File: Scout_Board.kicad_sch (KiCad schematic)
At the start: 0 parts

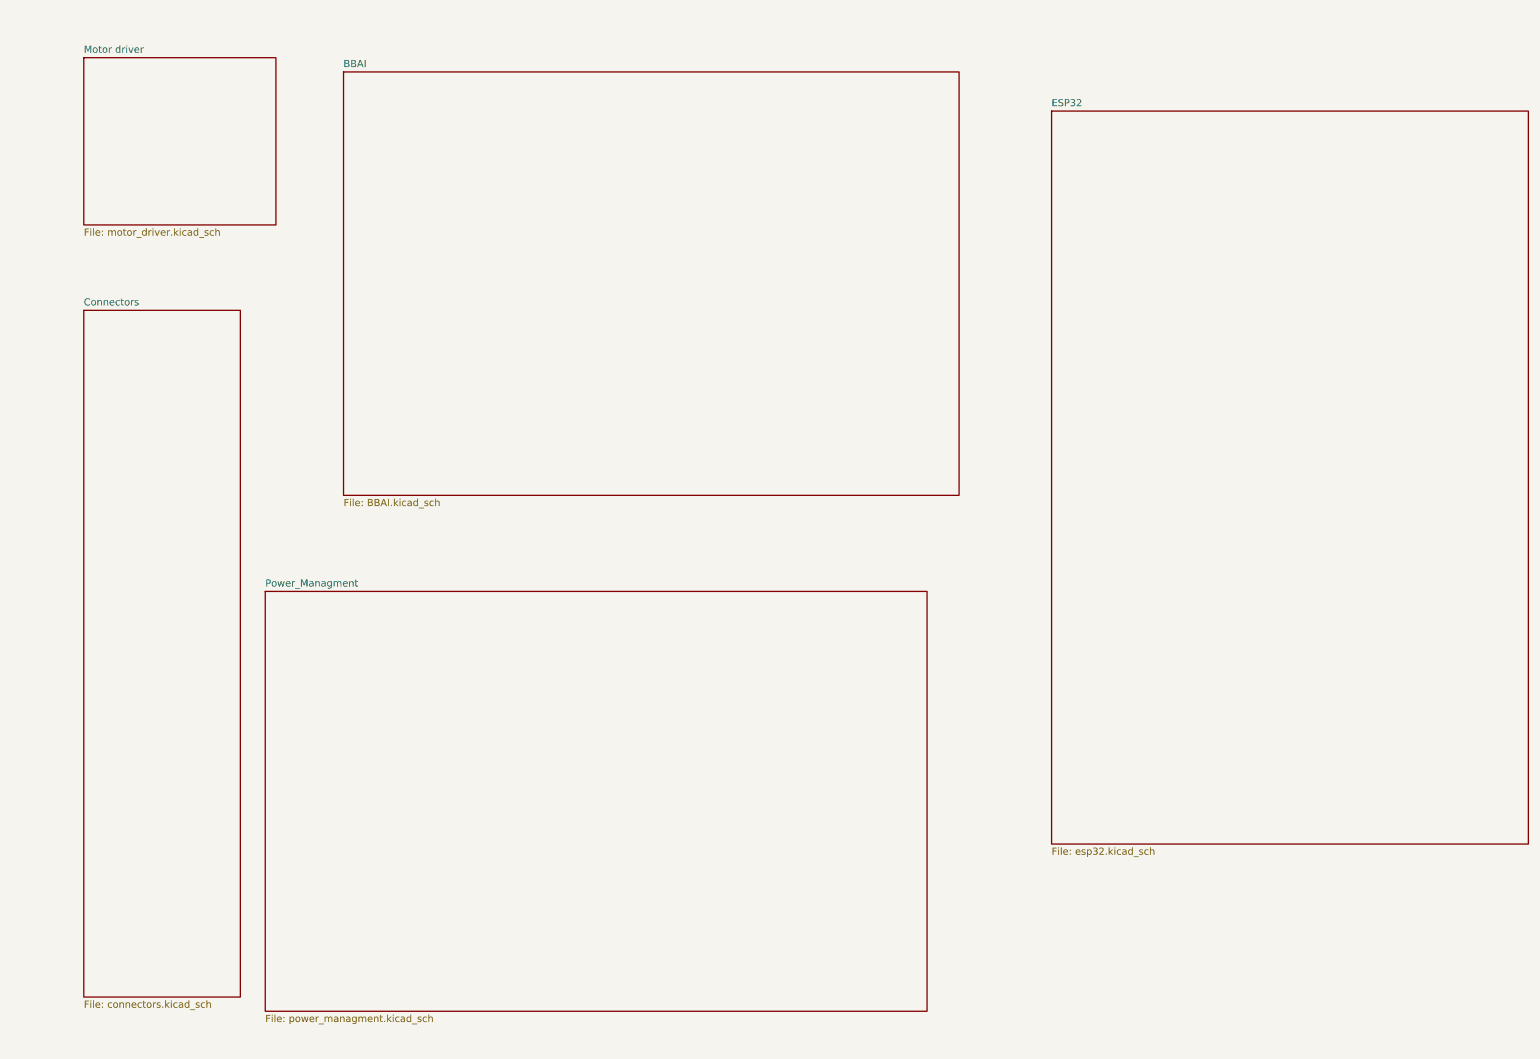
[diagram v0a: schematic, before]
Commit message: Base changes
Deleted the redundant files.
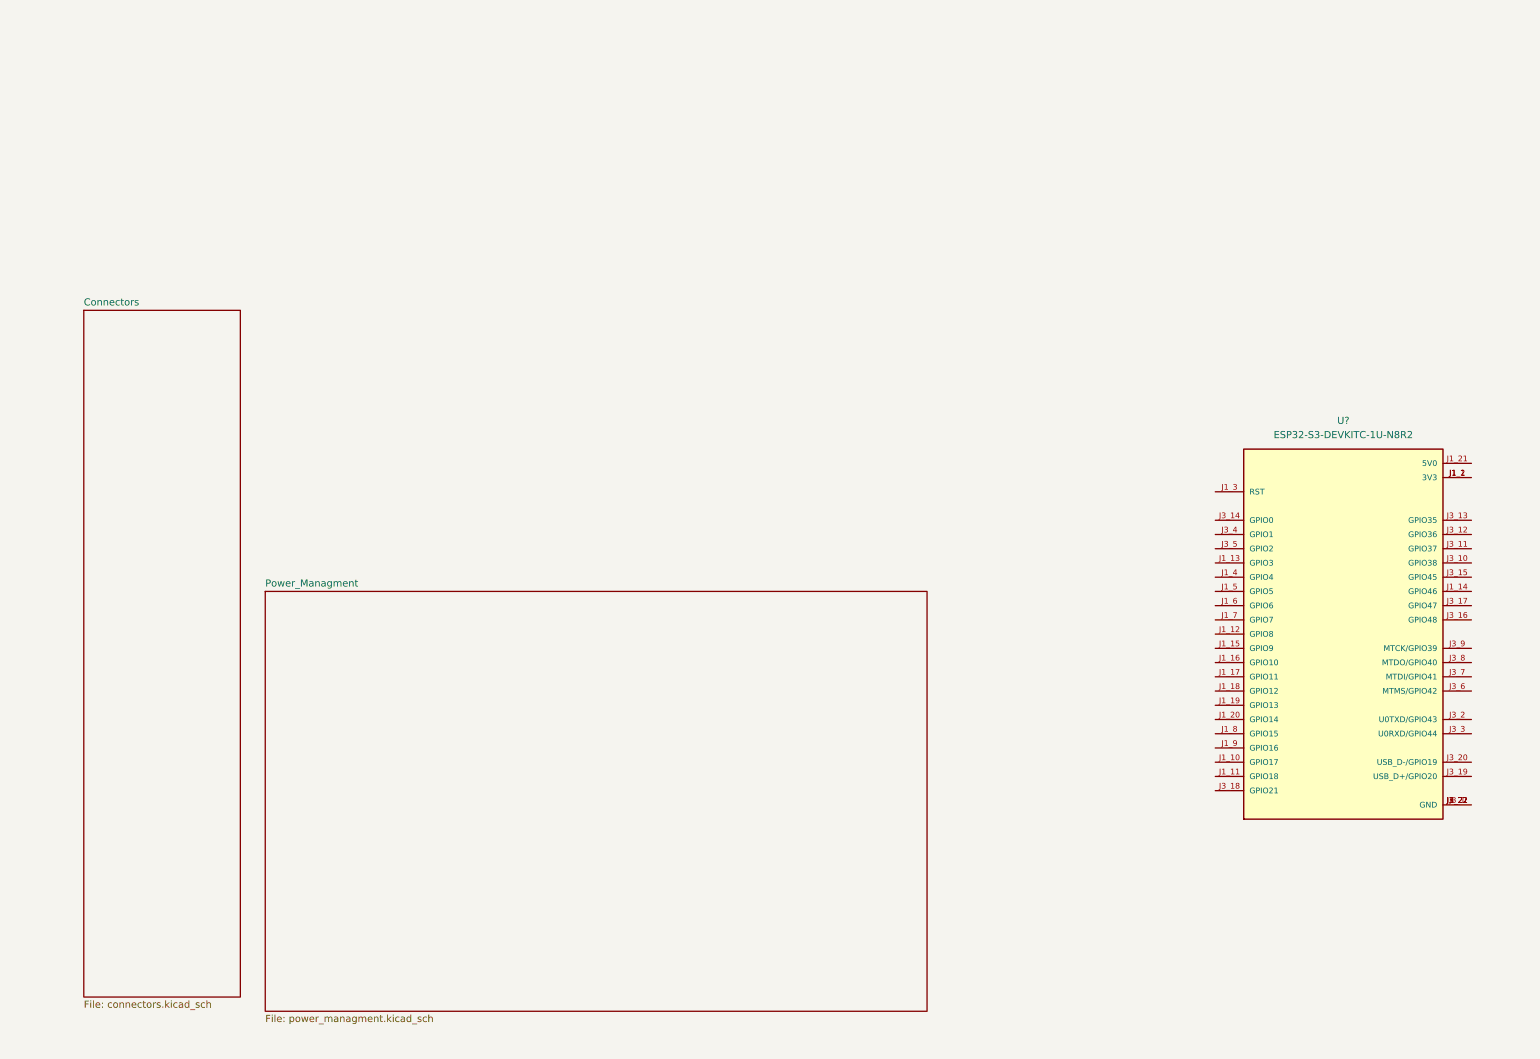
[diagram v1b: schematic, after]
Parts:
- added U?: ESP32-S3-DEVKITC-1U-N8R2, ESP32-S3-DEVKITC-1U-N8R2:XCVR_ESP32-S3-DEVKITC-1U-N8R2, symbol ESP32-S3-DEVKITC-1U-N8R2:ESP32-S3-DEVKITC-1U-N8R2
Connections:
- new net: U?.J1_1 (3V3), U?.J1_2 (3V3)
- new net: U?.J1_22 (GND), U?.J3_1 (GND), U?.J3_21 (GND), U?.J3_22 (GND)
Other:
- removed sheet BBAI
- removed sheet ESP32
- removed sheet Motor driver
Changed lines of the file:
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@@
 (kicad_sch (version 20230121) (generator eeschema)
   (paper "A4")
-  (sheet (at 191.77 28.575) (size 85.09 130.81) (fields_autoplaced)
-    (stroke (width 0.1524) (type solid))
-    (fill (color 0 0 0 0.0000))
-    (property "Sheetname" "ESP32" (at 191.77 27.8634 0)
-      (effects (font (size 1.27 1.27)) (justify left bottom))
+  (symbol (lib_id "ESP32-S3-DEVKITC-1U-N8R2:ESP32-S3-DEVKITC-1U-N8R2") (at 243.84 121.92 0) (unit 1)
+    (in_bom yes) (on_board yes) (dnp no) (fields_autoplaced)
+    (property "Reference" "U?" (at 243.84 83.82 0)
+      (effects (font (size 1.27 1.27)))
     )
-    (property "Sheetfile" "esp32.kicad_sch" (at 191.77 159.9696 0)
-      (effects (font (size 1.27 1.27)) (justify left top))
+    (property "Value" "ESP32-S3-DEVKITC-1U-N8R2" (at 243.84 86.36 0)
+      (effects (font (size 1.27 1.27)))
     )
+    (property "Footprint" "ESP32-S3-DEVKITC-1U-N8R2:XCVR_ESP32-S3-DEVKITC-1U-N8R2" (at 243.84 121.92 0)
+      (effects (font (size 1.27 1.27)) (justify bottom) hide)
+    )
+    (property "Datasheet" "" (at 243.84 121.92 0)
+      (effects (font (size 1.27 1.27)) hide)
+    )
+    (property "MF" "Espressif Systems" (at 243.84 121.92 0)
+      (effects (font (size 1.27 1.27)) (justify bottom) hide)
+    )
+    (property "MAXIMUM_PACKAGE_HEIGHT" "10.69mm" (at 243.84 121.92 0)
+      (effects (font (size 1.27 1.27)) (justify bottom) hide)
+    )
+    (property "Package" "None" (at 243.84 121.92 0)
+      (effects (font (size 1.27 1.27)) (justify bottom) hide)
+    )
+    (property "Price" "None" (at 243.84 121.92 0)
+      (effects (font (size 1.27 1.27)) (justify bottom) hide)
+    )
+    (property "Check_prices" "https://www.snapeda.com/parts/ESP32-S3-DEVKITC-1U-N8R2/Espressif+Systems/view-part/?ref=eda" (at 243.84 121.92 0)
+      (effects (font (size 1.27 1.27)) (justify bottom) hide)
+    )
+    (property "STANDARD" "Manufacturer Recommendations" (at 243.84 121.92 0)
+      (effects (font (size 1.27 1.27)) (justify bottom) hide)
+    )
+    (property "PARTREV" "5.3" (at 243.84 121.92 0)
+      (effects (font (size 1.27 1.27)) (justify bottom) hide)
+    )
+    (property "SnapEDA_Link" "https://www.snapeda.com/parts/ESP32-S3-DEVKITC-1U-N8R2/Espressif+Systems/view-part/?ref=snap" (at 243.84 121.92 0)
+      (effects (font (size 1.27 1.27)) (justify bottom) hide)
+    )
+    (property "MP" "ESP32-S3-DEVKITC-1U-N8R2" (at 243.84 121.92 0)
+      (effects (font (size 1.27 1.27)) (justify bottom) hide)
+    )
+    (property "Purchase-URL" "https://www.snapeda.com/api/url_track_click_mouser/?unipart_id=12089198&manufacturer=Espressif Systems&part_name=ESP32-S3-DEVKITC-1U-N8R2&search_term=esp32-s3-devkitc-1u" (at 243.84 121.92 0)
+      (effects (font (size 1.27 1.27)) (justify bottom) hide)
+    )
+    (property "Description" "\nWiFi Development Tools - 802.11 ESP32-S3 Gen-Purpose Dev Bd, embeds ESP32-S3-WROOM-1U-N8R2, 8 MB Quad Flash, 2 MB Quad PSRAM, IPEX antenna connector, w/ Pin Header\n" (at 243.84 121.92 0)
+      (effects (font (size 1.27 1.27)) (justify bottom) hide)
+    )
+    (property "Availability" "In Stock" (at 243.84 121.92 0)
+      (effects (font (size 1.27 1.27)) (justify bottom) hide)
+    )
+    (property "MANUFACTURER" "Espressif" (at 243.84 121.92 0)
+      (effects (font (size 1.27 1.27)) (justify bottom) hide)
+    )
+    (pin "J1_10")
+    (pin "J3_18")
+    (pin "J3_7")
+    (pin "J3_4")
+    (pin "J1_13")
+    (pin "J3_3")
+    (pin "J3_15")
+    (pin "J3_11")
+    (pin "J3_16")
+    (pin "J1_8")
+    (pin "J3_19")
+    (pin "J3_2")
+    (pin "J1_3")
+    (pin "J3_9")
+    (pin "J3_6")
+    (pin "J3_17")
+    (pin "J3_22")
+    (pin "J1_4")
+    (pin "J3_1")
+    (pin "J1_14")
+    (pin "J1_20")
+    (pin "J1_5")
+    (pin "J1_18")
+    (pin "J1_2")
+    (pin "J1_16")
+    (pin "J1_17")
+    (pin "J3_14")
+    (pin "J3_12")
+    (pin "J1_7")
+    (pin "J3_20")
+    (pin "J1_11")
+    (pin "J1_15")
+    (pin "J1_19")
+    (pin "J1_12")
+    (pin "J1_21")
+    (pin "J3_5")
+    (pin "J1_22")
+    (pin "J3_8")
+    (pin "J3_10")
+    (pin "J1_9")
+    (pin "J3_13")
+    (pin "J1_6")
+    (pin "J1_1")
+    (pin "J3_21")
     (instances
       (project "Scout_Board"
-        (path "/e58a9779-147f-4c0c-a745-6e9bc8ec0357" (page "4"))
+        (path "/e58a9779-147f-4c0c-a745-6e9bc8ec0357"
+          (reference "U?") (unit 1)
+        )
       )
     )
@@
     )
   )
-  (sheet (at 19.05 19.05) (size 34.29 29.845) (fields_autoplaced)
-    (stroke (width 0.1524) (type solid))
-    (fill (color 0 0 0 0.0000))
-    (property "Sheetname" "Motor driver" (at 19.05 18.3384 0)
-      (effects (font (size 1.27 1.27)) (justify left bottom))
-    )
-    (property "Sheetfile" "motor_driver.kicad_sch" (at 19.05 49.4796 0)
-      (effects (font (size 1.27 1.27)) (justify left top))
-    )
-    (instances
-      (project "Scout_Board"
-        (path "/e58a9779-147f-4c0c-a745-6e9bc8ec0357" (page "6"))
-      )
-    )
-  )
   (sheet (at 19.05 64.135) (size 27.94 122.555) (fields_autoplaced)
     (stroke (width 0.1524) (type solid))
@@
       )
     )
-  )
-  (sheet (at 65.405 21.59) (size 109.855 75.565) (fields_autoplaced)
-    (stroke (width 0.1524) (type solid))
-    (fill (color 0 0 0 0.0000))
-    (property "Sheetname" "BBAI" (at 65.405 20.8784 0)
-      (effects (font (size 1.27 1.27)) (justify left bottom))
-    )
-    (property "Sheetfile" "BBAI.kicad_sch" (at 65.405 97.7396 0)
-      (effects (font (size 1.27 1.27)) (justify left top))
-    )
-    (instances
-      (project "Scout_Board"
-        (path "/e58a9779-147f-4c0c-a745-6e9bc8ec0357" (page "2"))
-      )
-    )

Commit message: In process of adding top and bottom lights
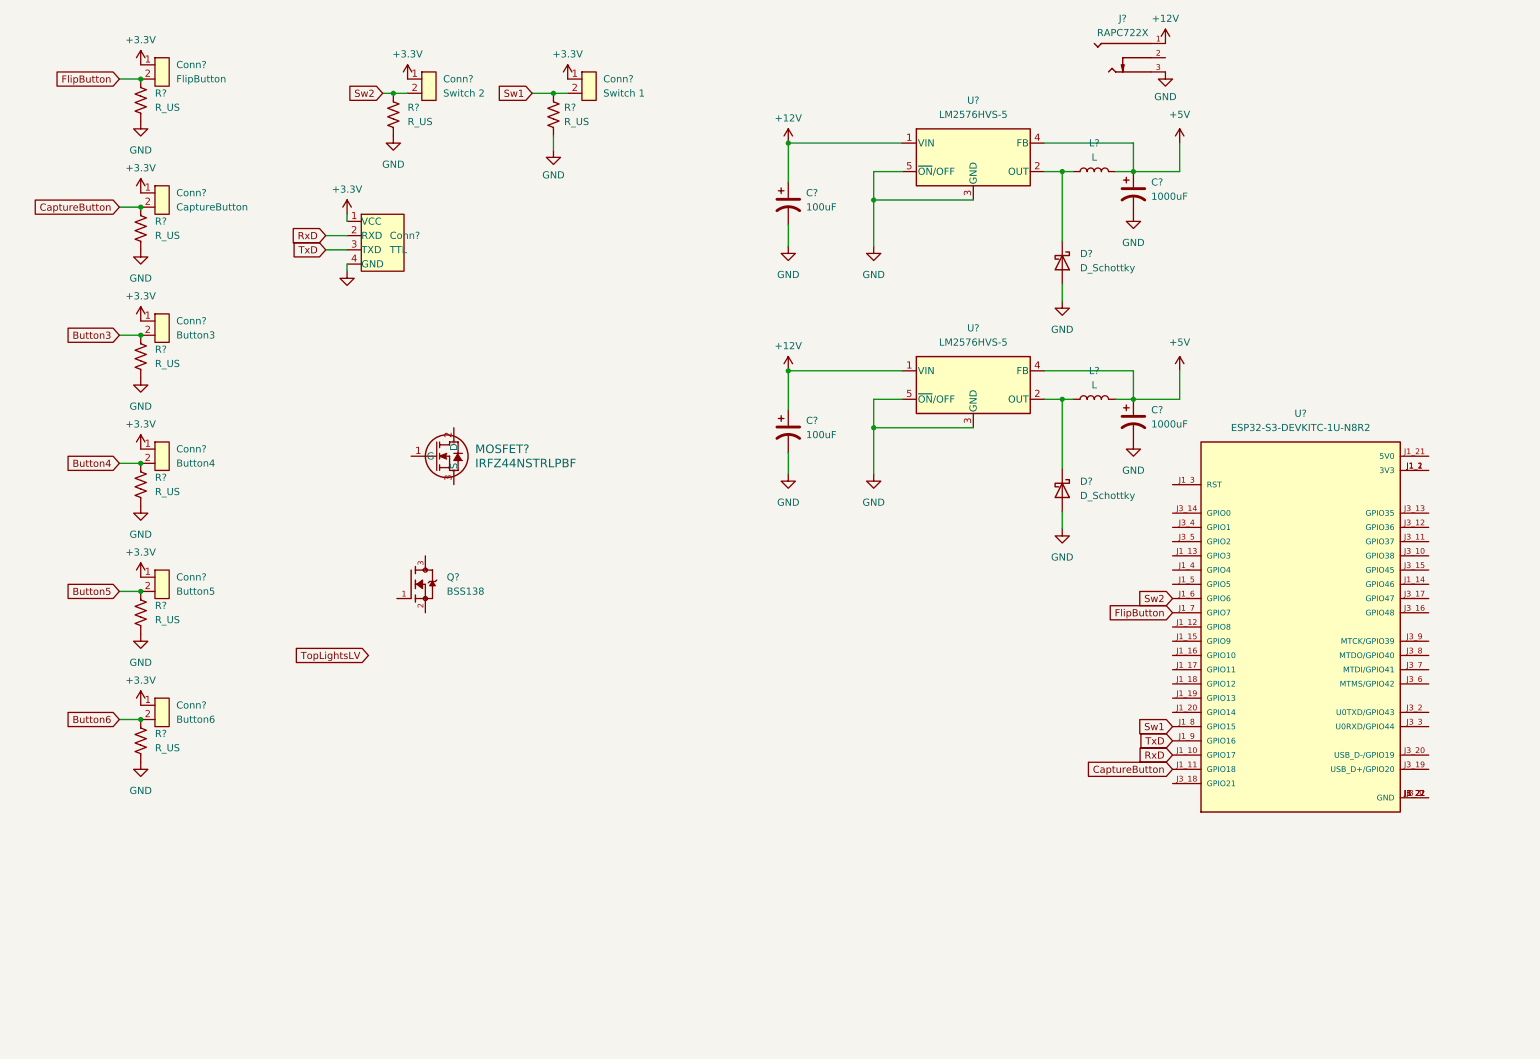
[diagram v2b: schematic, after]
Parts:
- added C? (x2): 100uF, symbol Device:C_Polarized_US
- added C? (x2): 1000uF, symbol Device:C_Polarized_US
- added Conn?: Button3, symbol Scout_library:B2B_VERT_1.5MM
- added Conn?: Switch 2, symbol Scout_library:B2B_VERT_1.5MM
- added Conn?: Button4, symbol Scout_library:B2B_VERT_1.5MM
- added Conn?: FlipButton, symbol Scout_library:B2B_VERT_1.5MM
- added Conn?: CaptureButton, symbol Scout_library:B2B_VERT_1.5MM
- added Conn?: Switch 1, symbol Scout_library:B2B_VERT_1.5MM
- added Conn?: TTL, symbol Scout_library:B4B_VERT_1.5MM
- added Conn?: Button6, symbol Scout_library:B2B_VERT_1.5MM
- added Conn?: Button5, symbol Scout_library:B2B_VERT_1.5MM
- added D? (x2): D_Schottky, symbol Device:D_Schottky
- added J?: RAPC722X, RAPC722X:SWITCHCRAFT_RAPC722X, symbol RAPC722X:RAPC722X
- added L? (x2): L, symbol Device:L
- added MOSFET?: IRFZ44NSTRLPBF, Downloaded_footprints:D2PAK_INF, symbol 2024-05-21_14-07-33:IRFZ44NSTRLPBF
- added Q?: BSS138, BSS138:SOT95P240X111-3N, symbol BSS138:BSS138
- added R? (x8): R_US, symbol Device:R_US
- added U? (x2): LM2576HVS-5, Package_TO_SOT_SMD:TO-263-5_TabPin3, symbol Regulator_Switching:LM2576HVS-5
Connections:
- net RxD: now reaches U?.J1_10 (GPIO17)
- net RxD: now also Conn?.2 (RXD)
- net CaptureButton: now reaches U?.J1_11 (GPIO18)
- net CaptureButton: now also Conn?.2 (Pin_2), R?.1
- net Sw2: now reaches U?.J1_6 (GPIO6)
- net Sw2: now also Conn?.2 (Pin_2), R?.1
- net FlipButton: now reaches U?.J1_7 (GPIO7)
- net FlipButton: now also Conn?.2 (Pin_2), R?.1
- net Sw1: now reaches U?.J1_8 (GPIO15)
- net Sw1: now also Conn?.2 (Pin_2), R?.1
- net TxD: now reaches U?.J1_9 (GPIO16)
- net TxD: now also Conn?.3 (TXD)
- new net: D?.1 (K), L?.1, U?.2 (OUT) (x2)
- new net +12V: C?.1, C?.1, J?.1, U?.1 (VIN), U?.1 (VIN)
- new net +3.3V: Conn?.1 (Pin_1), Conn?.1 (Pin_1), Conn?.1 (Pin_1), Conn?.1 (Pin_1), Conn?.1 (Pin_1), Conn?.1 (Pin_1), Conn?.1 (Pin_1), Conn?.1 (Pin_1), Conn?.1 (VCC)
- new net +5V: C?.1, C?.1, L?.2, L?.2, U?.4 (FB), U?.4 (FB)
- new net Button3: Conn?.2 (Pin_2), R?.1
- new net Button4: Conn?.2 (Pin_2), R?.1
- new net Button5: Conn?.2 (Pin_2), R?.1
- new net Button6: Conn?.2 (Pin_2), R?.1
- new net GND: C?.2, C?.2, C?.2, C?.2, Conn?.4 (GND), D?.2 (A), D?.2 (A), J?.3, R?.2, R?.2, R?.2, R?.2, R?.2, R?.2, R?.2, R?.2, U?.3 (GND), U?.3 (GND), U?.5 (~{ON}/OFF), U?.5 (~{ON}/OFF)
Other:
- removed sheet Connectors
- removed sheet Power_Managment
- moved on the sheet: U?
